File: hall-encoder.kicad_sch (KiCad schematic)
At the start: 1 part, among them U8 MLX90395xLW

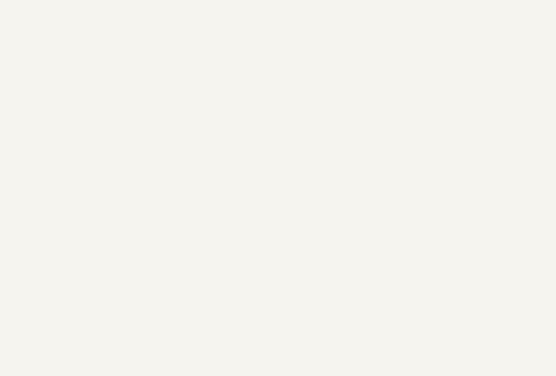
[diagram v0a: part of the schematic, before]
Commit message: feat: done rough board placements for general shape
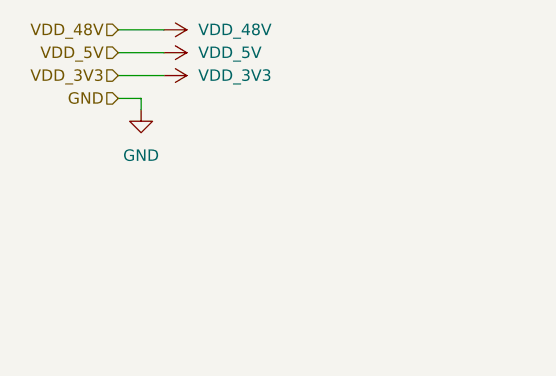
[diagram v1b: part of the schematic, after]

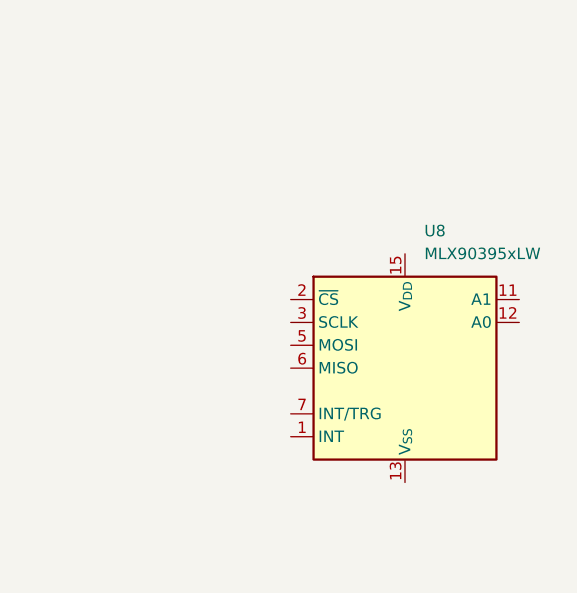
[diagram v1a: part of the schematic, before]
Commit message: fix: update fpga with power supply
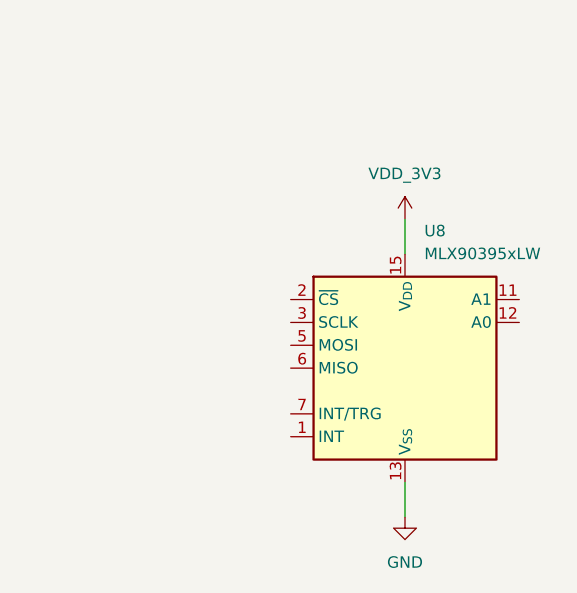
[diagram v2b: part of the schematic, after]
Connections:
- net GND: now also U8.10 (V_{SS}), U8.13 (V_{SS}), U8.14 (V_{SS}), U8.16 (V_{SS}), U8.17 (V_{SS}), U8.4 (V_{SS}), U8.8 (V_{SS}), U8.9 (V_{SS})
- net VDD_3V3: now also U8.15 (V_{DD})
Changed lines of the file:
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@@
+	(wire
+		(pts
+			(xy 143.51 114.3) (xy 143.51 118.11)
+		)
+		(stroke
+			(width 0)
+			(type default)
+		)
+	)
 	(wire
 		(pts
@@
 		(pts
 			(xy 26.67 16.51) (xy 31.75 16.51)
+		)
+		(stroke
+			(width 0)
+			(type default)
+		)
+	)
+	(wire
+		(pts
+			(xy 143.51 85.09) (xy 143.51 88.9)
 		)
 		(stroke
@@
 					(unit 1)
 				)
+			)
+		)
+	)
+	(symbol
+		(lib_id "power:GND")
+		(at 143.51 118.11 0)
+		(unit 1)
+		(exclude_from_sim no)
+		(in_bom yes)
+		(on_board yes)
+		(dnp no)
+		(fields_autoplaced yes)
+		(property "Reference" "#PWR0120"
+			(at 143.51 124.46 0)
+			(effects
+				(font
+					(size 1.27 1.27)
+				)
+				(hide yes)
+			)
+		)
+		(property "Value" "GND"
+			(at 143.51 123.19 0)
+			(effects
+				(font
+					(size 1.27 1.27)
+				)
+			)
+		)
+		(property "Footprint" ""
+			(at 143.51 118.11 0)
+			(effects
+				(font
+					(size 1.27 1.27)
+				)
+				(hide yes)
+			)
+		)
+		(property "Datasheet" ""
+			(at 143.51 118.11 0)
+			(effects
+				(font
+					(size 1.27 1.27)
+				)
+				(hide yes)
+			)
+		)
+		(property "Description" "Power symbol creates a global label with name \"GND\" , ground"
+			(at 143.51 118.11 0)
+			(effects
+				(font
+					(size 1.27 1.27)
+				)
+				(hide yes)
+			)
+		)
+		(pin "1"
+		)
+		(instances
+			(project "kicad-template-project"
+				(path "/e1f256b3-686f-4e34-9512-fa5de8536fd7/239aab14-7c61-4378-98ce-e28ed823006b"
+					(reference "#PWR0120")
+					(unit 1)
+				)
+			)
+		)
+	)
+	(symbol
+		(lib_id "power:VDD")
+		(at 143.51 85.09 0)
+		(unit 1)
+		(exclude_from_sim no)
+		(in_bom yes)
+		(on_board yes)
+		(dnp no)
+		(fields_autoplaced yes)
+		(property "Reference" "#PWR0121"
+			(at 143.51 88.9 0)
+			(effects
+				(font
+					(size 1.27 1.27)
+				)
+				(hide yes)
+			)
+		)
+		(property "Value" "VDD_3V3"
+			(at 143.51 80.01 0)
+			(effects
+				(font
+					(size 1.27 1.27)
+				)
+			)
+		)
+		(property "Footprint" ""
+			(at 143.51 85.09 0)
+			(effects
+				(font
+					(size 1.27 1.27)
+				)
+				(hide yes)
+			)
+		)
+		(property "Datasheet" ""
+			(at 143.51 85.09 0)
+			(effects
+				(font
+					(size 1.27 1.27)
+				)
+				(hide yes)
+			)
+		)
+		(property "Description" "Power symbol creates a global label with name \"VDD\""
+			(at 143.51 85.09 0)
+			(effects
+				(font
+					(size 1.27 1.27)
+				)
+				(hide yes)
+			)
+		)
+		(property "MFR_PN1" ""
+			(at 143.51 85.09 0)
+			(effects
+				(font
+					(size 1.27 1.27)
+				)
+				(hide yes)
+			)
+		)
+		(property "MFR_PN2" ""
+			(at 143.51 85.09 0)
+			(effects
+				(font
+					(size 1.27 1.27)
+				)
+				(hide yes)
+			)
+		)
+		(property "MFR_PN3" ""
+			(at 143.51 85.09 0)
+			(effects
+				(font
+					(size 1.27 1.27)
+				)
+				(hide yes)
+			)
+		)
+		(property "JLC_PN" ""
+			(at 143.51 85.09 0)
+			(effects
+				(font
+					(size 1.27 1.27)
+				)
+				(hide yes)
+			)
+		)
+		(pin "1"
+		)
+		(instances
+			(project "kicad-template-project"
+				(path "/e1f256b3-686f-4e34-9512-fa5de8536fd7/239aab14-7c61-4378-98ce-e28ed823006b"
+					(reference "#PWR0121")
+					(unit 1)
+				)

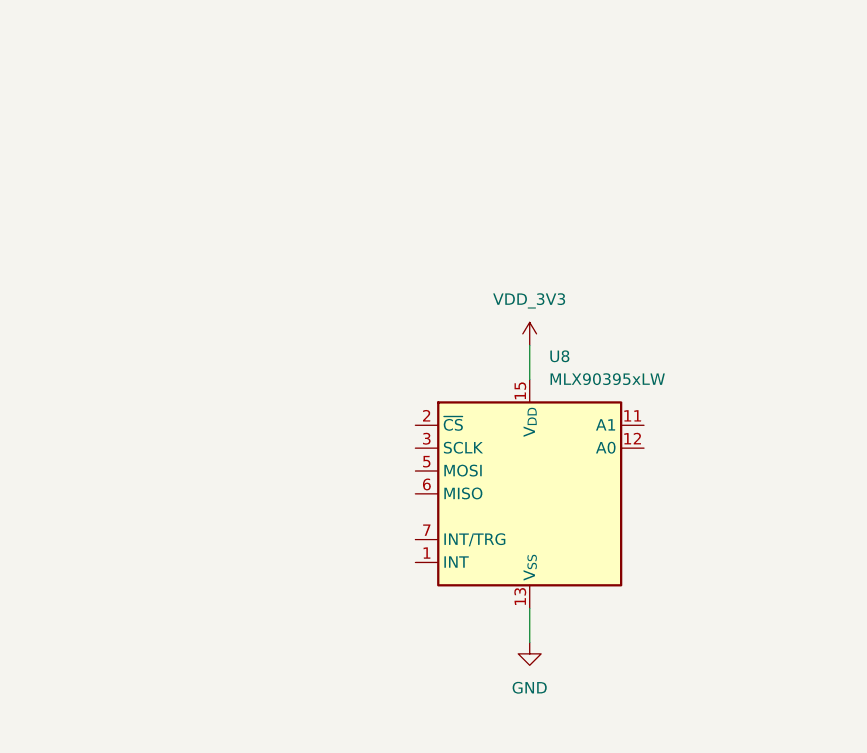
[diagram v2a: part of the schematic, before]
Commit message: fix: fleshignout schematic for mcu, fpga and mag + peripherals
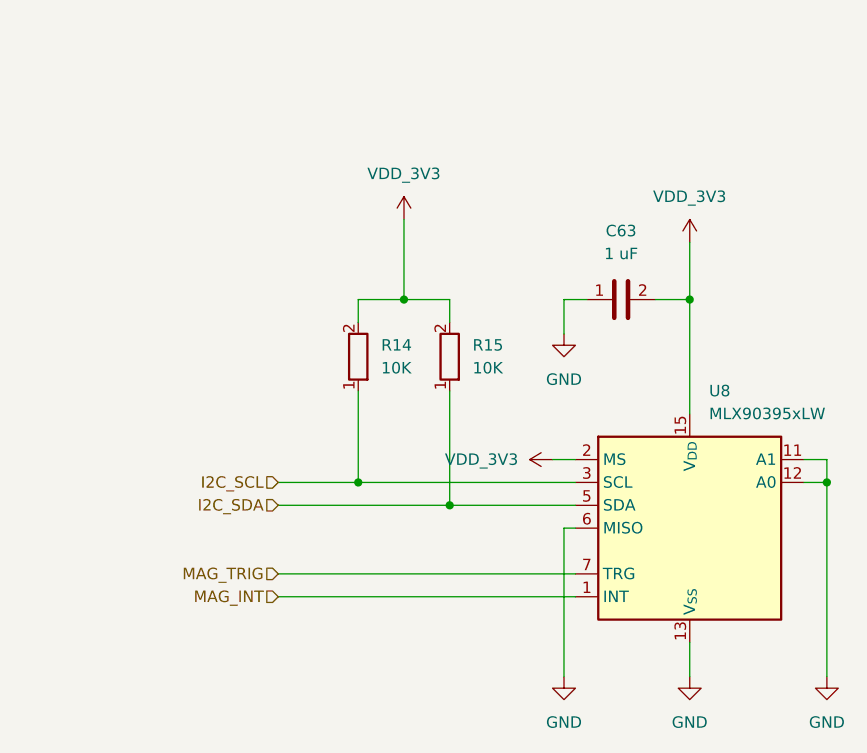
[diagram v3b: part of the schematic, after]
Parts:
- added C63: 1 uF, chenry-footprint-lib:C_0402, symbol 0-chenry-component-lib:C_0402_1U
- added R14, R15: 10K, chenry-footprint-lib:R_0402, symbol 0-chenry-component-lib:R_0402_10K
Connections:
- net GND: now also U8.11 (A1), U8.12 (A0), U8.6 (MISO), C63.1
- net VDD_3V3: now also U8.2 (~{CS}), C63.2, R14.2, R15.2
- net MAG_INT: now reaches U8.1 (INT)
- net I2C_SCL: now reaches U8.3 (SCLK)
- net I2C_SCL: now also R14.1
- net I2C_SDA: now reaches U8.5 (MOSI)
- net I2C_SDA: now also R15.1
- net MAG_TRIG: now reaches U8.7 (INT/TRG)
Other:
- moved on the sheet: U8
